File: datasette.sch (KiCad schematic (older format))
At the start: 32 parts, among them CN3 CASSETTE, CN7 SERIAL_BUS, Q5 2SD880, U11 74LS125, U9 74LS06

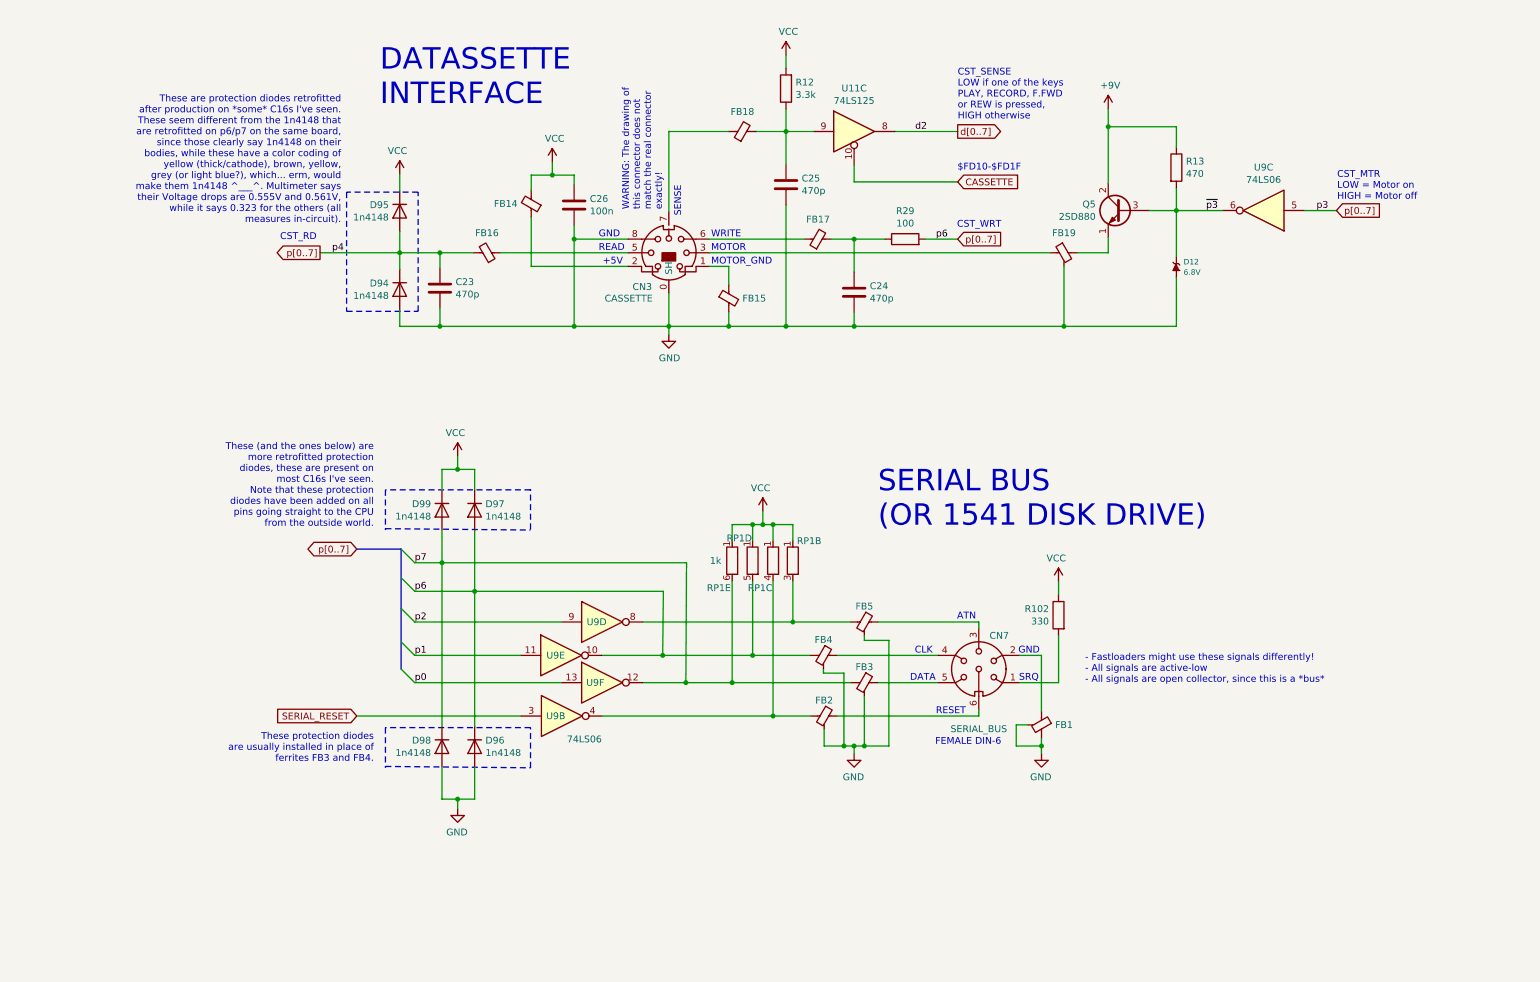
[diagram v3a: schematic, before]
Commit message: Add diode+resistor to control Datassette motor when using 6510
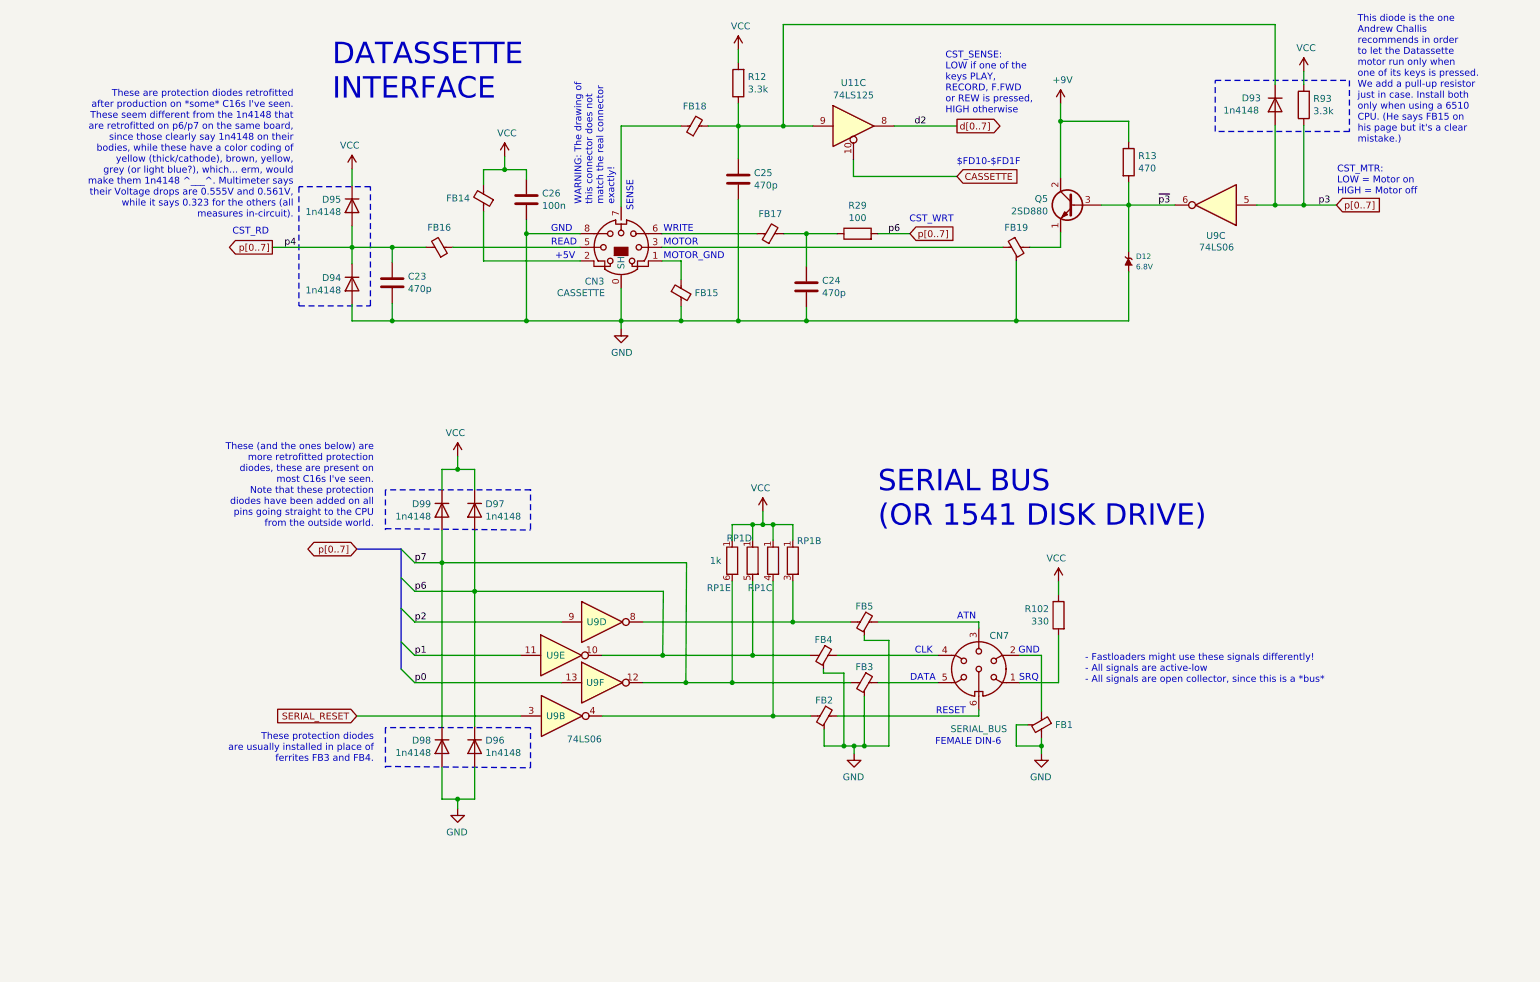
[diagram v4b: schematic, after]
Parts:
- added D93: 1n4148, Diode_THT:D_DO-35_SOD27_P5.08mm_Vertical_KathodeUp, symbol Device:D
- added R93: 3.3k, Resistor_THT:R_Axial_DIN0207_L6.3mm_D2.5mm_P5.08mm_Vertical, symbol Device:R
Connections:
- net VCC: now also R93.2
- net p[0..7]: now also D93.2 (A), R93.1
- net at C25.2, FB18.2, R12.1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: now also D93.1 (K)
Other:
- note added: "CST_MTR:\nLOW = Motor on\nHIGH = Motor off"
- note added: "CST_SENSE:\nLOW if one of the\nkeys PLAY,\nRECORD, F.FWD\nor REW is pressed,\nHIGH otherwise"
- note added: "This diode is the one\nAndrew Challis\nrecommends in order\nto let the Datassette\nmotor run only when\none of its keys is pressed.\nWe add a pull-up resistor\njust in case. Install both\nonly when using a 6510\nCPU. (He says FB15 on\nhis page but it's a clear\nmistake.)"
- note removed: "CST_MTR\nLOW = Motor on\nHIGH = Motor off"
- note removed: "CST_SENSE\nLOW if one of the keys\nPLAY, RECORD, F.FWD\nor REW is pressed,\nHIGH otherwise"
- moved on the sheet: C23, C24, C25, C26, CN3, D12, D94, D95, FB14, FB15, FB16, FB17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

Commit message: Add better ESD protection for Serial Connector
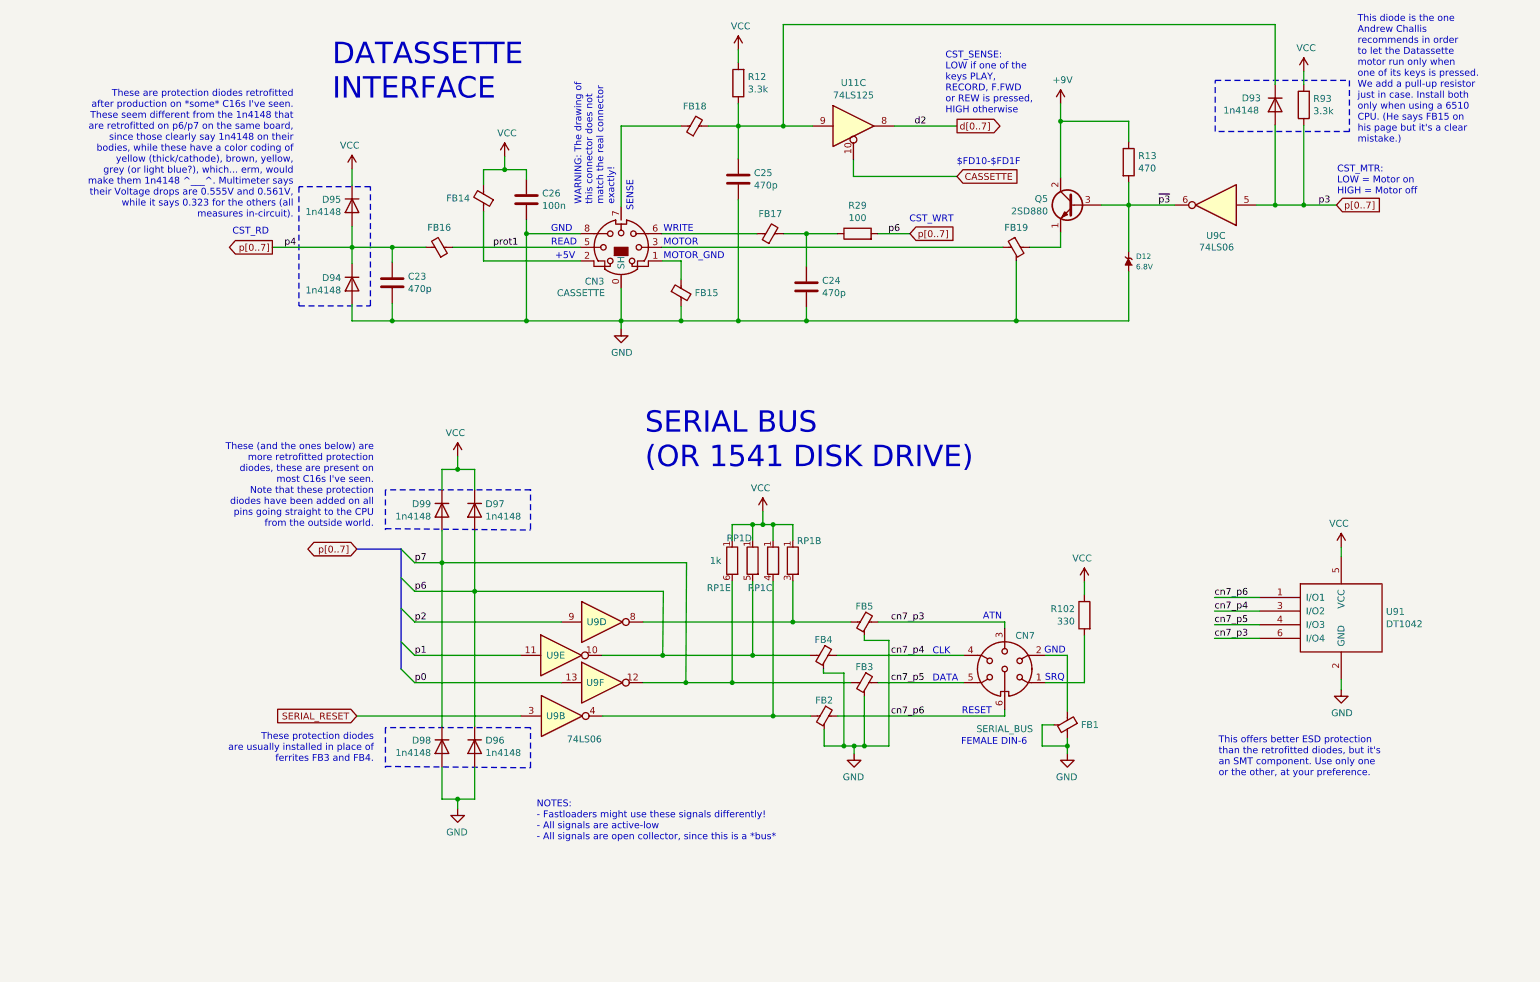
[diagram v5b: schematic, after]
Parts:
- added U91: DT1042, Package_SO:TSOP-6_1.65x3.05mm_P0.95mm, symbol DT1042:DT1042
- D96, D97, D98, D99: Notes (none) -> Do not mount if U91 is mounted
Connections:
- net GND: now also U91.2 (GND)
- net VCC: now also U91.5 (VCC)
- net cn7_p5: now reaches CN7.5, FB3.1
- net cn7_p5: now also U91.4 (I/O3)
- net cn7_p6: now reaches CN7.6, FB2.1
- net cn7_p6: now also U91.1 (I/O1)
- net cn7_p4: now reaches CN7.4, FB4.1
- net cn7_p4: now also U91.3 (I/O2)
- net cn7_p3: now reaches CN7.3, FB5.1
- net cn7_p3: now also U91.6 (I/O4)
- net prot1: now reaches CN3.5, FB16.1
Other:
- note added: "NOTES:\n- Fastloaders might use these signals differently!\n- All signals are active-low\n- All signals are open collector, since this is a *bus*"
- note added: "This offers better ESD protection\nthan the retrofitted diodes, but it's\nan SMT component. Use only one\nor the other, at your preference."
- note removed: "- Fastloaders might use these signals differently!\n- All signals are active-low\n- All signals are open collector, since this is a *bus*"
- moved on the sheet: CN7, FB1, R102
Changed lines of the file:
@@
 p3
 Wire Wire Line
-	7900 5620 7900 5275
+	8090 5620 8090 5275
 $Comp
 L Device:R R102
 U 1 1 5ED6F117
-P 7900 5125
-F 0 "R102" H 7970 5171 50  0000 L CNN
-F 1 "330" H 7970 5080 50  0000 L CNN
-F 2 "Resistor_THT:R_Axial_DIN0207_L6.3mm_D2.5mm_P5.08mm_Vertical" V 7830 5125 50  0001 C CNN
-F 3 "~" H 7900 5125 50  0001 C CNN
-	1    7900 5125
+P 8090 5125
+F 0 "R102" H 8160 5171 50  0000 L CNN
+F 1 "330" H 8160 5080 50  0000 L CNN
+F 2 "Resistor_THT:R_Axial_DIN0207_L6.3mm_D2.5mm_P5.08mm_Vertical" V 8020 5125 50  0001 C CNN
+F 3 "~" H 8090 5125 50  0001 C CNN
+	1    8090 5125
 	-1   0    0    -1
 $EndComp
@@
 L power:VCC #PWR0157
 U 1 1 5ED6F7A0
-P 7900 4880
-F 0 "#PWR0157" H 7900 4730 50  0001 C CNN
-F 1 "VCC" H 7917 5053 50  0000 C CNN
-F 2 "" H 7900 4880 50  0001 C CNN
-F 3 "" H 7900 4880 50  0001 C CNN
-	1    7900 4880
-	-1   0    0    -1
-$EndComp
-Wire Wire Line
-	7900 4880 7900 4975
-Text Notes 6995 6085 0    50   ~ 0
+P 8090 4880
+F 0 "#PWR0157" H 8090 4730 50  0001 C CNN
+F 1 "VCC" H 8107 5053 50  0000 C CNN
+F 2 "" H 8090 4880 50  0001 C CNN
+F 3 "" H 8090 4880 50  0001 C CNN
+	1    8090 4880
+	-1   0    0    -1
+$EndComp
+Wire Wire Line
+	8090 4880 8090 4975
+Text Notes 7185 6085 0    50   ~ 0
 FEMALE DIN-6
 Wire Wire Line
-	7315 5175 6575 5175
+	7505 5175 6575 5175
 $Comp
 L 74xx:74LS06 U9
@@
 	4250 5175 3175 5175
 Wire Wire Line
-	7315 5865 6280 5865
+	7505 5865 6280 5865
 Wire Wire Line
 	6080 5865 5805 5865
@@
 Wire Wire Line
 	3955 5865 2750 5865
-Text Notes 6575 4490 0    157  ~ 0
+Text Notes 4865 4060 0    157  ~ 0
 SERIAL BUS\n(OR 1541 DISK DRIVE)
 Text Notes 2570 1355 0    157  ~ 0
@@
 	6400 6085 6325 6085
 Wire Wire Line
-	7315 5820 7315 5865
-Wire Wire Line
-	7015 5620 6575 5620
-Wire Wire Line
-	7015 5420 6275 5420
-Wire Wire Line
-	7315 5220 7315 5175
-Wire Wire Line
-	7775 5420 7615 5420
-Wire Wire Line
-	7615 5620 7900 5620
-Wire Wire Line
-	7775 6085 7775 6140
-Connection ~ 7775 6085
-Wire Wire Line
-	7590 6085 7775 6085
-Wire Wire Line
-	7590 5930 7590 6085
-Wire Wire Line
-	7675 5930 7590 5930
+	7505 5820 7505 5865
+Wire Wire Line
+	7205 5620 6575 5620
+Wire Wire Line
+	7205 5420 6275 5420
+Wire Wire Line
+	7505 5220 7505 5175
+Wire Wire Line
+	7965 5420 7805 5420
+Wire Wire Line
+	7805 5620 8090 5620
+Wire Wire Line
+	7965 6085 7965 6140
+Connection ~ 7965 6085
+Wire Wire Line
+	7780 6085 7965 6085
+Wire Wire Line
+	7780 5930 7780 6085
+Wire Wire Line
+	7865 5930 7780 5930
 $Comp
 L Ferrite3Pin:Ferrite_3pin FB1
 U 1 1 5E2BCB55
-P 7775 5930
-F 0 "FB1" H 7675 5930 50  0000 R CNN
-F 1 "Ferrite_3pin" V 7629 5930 50  0001 C CNN
-F 2 "LittleSixteen:Ferrite" V 7705 5930 50  0001 C CNN
-F 3 "~" H 7775 5930 50  0001 C CNN
-	1    7775 5930
+P 7965 5930
+F 0 "FB1" H 7865 5930 50  0000 R CNN
+F 1 "Ferrite_3pin" V 7819 5930 50  0001 C CNN
+F 2 "LittleSixteen:Ferrite" V 7895 5930 50  0001 C CNN
+F 3 "~" H 7965 5930 50  0001 C CNN
+	1    7965 5930
 	-1   0    0    -1
 $EndComp
@@
 L power:GND #PWR0158
 U 1 1 5ED75A9A
-P 7775 6140
-F 0 "#PWR0158" H 7775 5890 50  0001 C CNN
-F 1 "GND" H 7780 5967 50  0000 C CNN
-F 2 "" H 7775 6140 50  0001 C CNN
-F 3 "" H 7775 6140 50  0001 C CNN
-	1    7775 6140
-	-1   0    0    -1
-$EndComp
-Wire Wire Line
-	7775 6030 7775 6085
-Wire Wire Line
-	7775 5830 7775 5420
+P 7965 6140
+F 0 "#PWR0158" H 7965 5890 50  0001 C CNN
+F 1 "GND" H 7970 5967 50  0000 C CNN
+F 2 "" H 7965 6140 50  0001 C CNN
+F 3 "" H 7965 6140 50  0001 C CNN
+	1    7965 6140
+	-1   0    0    -1
+$EndComp
+Wire Wire Line
+	7965 6030 7965 6085
+Wire Wire Line
+	7965 5830 7965 5420
 $Comp
 L Ferrite3Pin:Ferrite_3pin FB19
@@
 F 2 "Diode_THT:D_DO-35_SOD27_P5.08mm_Vertical_KathodeUp" H 3615 4355 50  0001 C CNN
 F 3 "~" H 3615 4355 50  0001 C CNN
+F 4 "Do not mount if U91 is mounted" H 3615 4355 50  0001 C CNN "Notes"
 	1    3615 4355
 	0    -1   1    0
@@
 Text Notes 2285 2215 2    50   ~ 0
 These are protection diodes retrofitted\nafter production on *some* C16s I've seen.\nThese seem different from the 1n4148 that\nare retrofitted on p6/p7 on the same board,\nsince those clearly say 1n4148 on their\nbodies, while these have a color coding of\nyellow (thick/cathode), brown, yellow,\ngrey (or light blue?), which... erm, would\nmake them 1n4148 ^___^. Multimeter says\ntheir Voltage drops are 0.555V and 0.561V,\nwhile it says 0.323 for the others (all\nmeasures in-circuit).
-Text Notes 7610 5615 0    50   ~ 0
+Text Notes 7800 5615 0    50   ~ 0
 SRQ
-Text Notes 7155 5165 0    50   ~ 0
+Text Notes 7345 5165 0    50   ~ 0
 ATN
-Text Notes 6845 5415 0    50   ~ 0
+Text Notes 6975 5420 0    50   ~ 0
 CLK
-Text Notes 6810 5615 0    50   ~ 0
+Text Notes 6975 5620 0    50   ~ 0
 DATA
-Text Notes 7000 5860 0    50   ~ 0
+Text Notes 7190 5860 0    50   ~ 0
 RESET
 $Comp
 L Connector:DIN-6 CN7
 U 1 1 5ED6C96C
-P 7315 5520
-F 0 "CN7" H 7165 5765 50  0000 C CNN
-F 1 "SERIAL_BUS" H 7315 5080 50  0000 C CNN
-F 2 "CommodorePlus4:Connector_DIN_Female_6Pin_3rows" H 7315 5520 50  0001 C CNN
-F 3 "http://www.mouser.com/ds/2/18/40_c091_abd_e-75918.pdf" H 7315 5520 50  0001 C CNN
-	1    7315 5520
-	-1   0    0    -1
-$EndComp
-Text Notes 7605 5415 0    50   ~ 0
+P 7505 5520
+F 0 "CN7" H 7355 5765 50  0000 C CNN
+F 1 "SERIAL_BUS" H 7505 5080 50  0000 C CNN
+F 2 "CommodorePlus4:Connector_DIN_Female_6Pin_3rows" H 7505 5520 50  0001 C CNN
+F 3 "http://www.mouser.com/ds/2/18/40_c091_abd_e-75918.pdf" H 7505 5520 50  0001 C CNN
+	1    7505 5520
+	-1   0    0    -1
+$EndComp
+Text Notes 7795 5415 0    50   ~ 0
 GND
-Text Notes 8095 5630 0    50   ~ 0
-- Fastloaders might use these signals differently!\n- All signals are active-low\n- All signals are open collector, since this is a *bus*
+Text Notes 4070 6785 0    50   ~ 0
+NOTES:\n- Fastloaders might use these signals differently!\n- All signals are active-low\n- All signals are open collector, since this is a *bus*
 Connection ~ 3010 2425
 Wire Notes Line
@@
 F 2 "Diode_THT:D_DO-35_SOD27_P5.08mm_Vertical_KathodeUp" H 3375 4355 50  0001 C CNN
 F 3 "~" H 3375 4355 50  0001 C CNN
+F 4 "Do not mount if U91 is mounted" H 3375 4355 50  0001 C CNN "Notes"
 	1    3375 4355
 	0    -1   1    0
@@
 F 2 "Diode_THT:D_DO-35_SOD27_P5.08mm_Vertical_KathodeUp" H 3615 6090 50  0001 C CNN
 F 3 "~" H 3615 6090 50  0001 C CNN
+F 4 "Do not mount if U91 is mounted" H 3615 6090 50  0001 C CNN "Notes"
 	1    3615 6090
 	0    -1   1    0
@@
 F 2 "Diode_THT:D_DO-35_SOD27_P5.08mm_Vertical_KathodeUp" H 3375 6090 50  0001 C CNN
 F 3 "~" H 3375 6090 50  0001 C CNN
+F 4 "Do not mount if U91 is mounted" H 3375 6090 50  0001 C CNN "Notes"
 	1    3375 6090
 	0    -1   1    0
@@
 Text Notes 10095 1665 0    50   ~ 0
 This diode is the one\nAndrew Challis\nrecommends in order\nto let the Datassette\nmotor run only when\none of its keys is pressed.\nWe add a pull-up resistor\njust in case. Install both\nonly when using a 6510\nCPU. (He says FB15 on\nhis page but it's a clear\nmistake.)
+$Comp
+L DT1042:DT1042 U91
+U 1 1 6223655A
+P 9975 5145
+F 0 "U91" H 10303 5191 50  0000 L CNN
+F 1 "DT1042" H 10303 5100 50  0000 L CNN
+F 2 "Package_SO:TSOP-6_1.65x3.05mm_P0.95mm" H 9825 4595 50  0001 C CNN
+F 3 "" H 9825 4595 50  0001 C CNN
+F 4 "Optional, protects Serial port from ESD" H 9975 5145 50  0001 C CNN "Notes"
+	1    9975 5145
+	1    0    0    -1
+$EndComp
+Wire Wire Line
+	9975 4695 9975 4625
+Wire Wire Line
+	9975 5595 9975 5670
+$Comp
+L power:VCC #PWR0209
+U 1 1 62244AD8
+P 9975 4625
+F 0 "#PWR0209" H 9975 4475 50  0001 C CNN
+F 1 "VCC" H 9992 4798 50  0000 C CNN
+F 2 "" H 9975 4625 50  0001 C CNN
+F 3 "" H 9975 4625 50  0001 C CNN
+	1    9975 4625
+	-1   0    0    -1
+$EndComp
+$Comp
+L power:GND #PWR0210
+U 1 1 6224539A
+P 9975 5670
+F 0 "#PWR0210" H 9975 5420 50  0001 C CNN
+F 1 "GND" H 9980 5497 50  0000 C CNN
+F 2 "" H 9975 5670 50  0001 C CNN
+F 3 "" H 9975 5670 50  0001 C CNN
+	1    9975 5670
+	1    0    0    -1
+$EndComp
+Wire Wire Line
+	9375 4995 9045 4995
+Wire Wire Line
+	9375 5095 9045 5095
+Wire Wire Line
+	9375 5195 9045 5195
+Wire Wire Line
+	9375 5295 9045 5295
+Text Label 3750 2425 0    50   ~ 0
+prot1
+Text Label 6670 5620 0    50   ~ 0
+cn7_p5
+Text Label 6670 5420 0    50   ~ 0
+cn7_p4
+Text Label 6670 5175 0    50   ~ 0
+cn7_p3
+Text Label 6670 5865 0    50   ~ 0
+cn7_p6
+Text Label 9045 5195 0    50   ~ 0
+cn7_p5
+Text Label 9045 5295 0    50   ~ 0
+cn7_p3
+Text Label 9045 5095 0    50   ~ 0
+cn7_p4
+Text Label 9045 4995 0    50   ~ 0
+cn7_p6
 Wire Bus Line
 	3075 4640 3075 5520
+Text Notes 9075 6315 0    50   ~ 0
+This offers better ESD protection\nthan the retrofitted diodes, but it's\nan SMT component. Use only one\nor the other, at your preference.
 $EndSCHEMATC
